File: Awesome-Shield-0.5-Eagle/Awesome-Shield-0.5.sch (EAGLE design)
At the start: 18 parts, among them J1 ARDUINO_R3_SHIELDUNO_R3_SHIEL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, P3 DNP, P4 DNP, SW1 SPST_TACT-EVQQ2

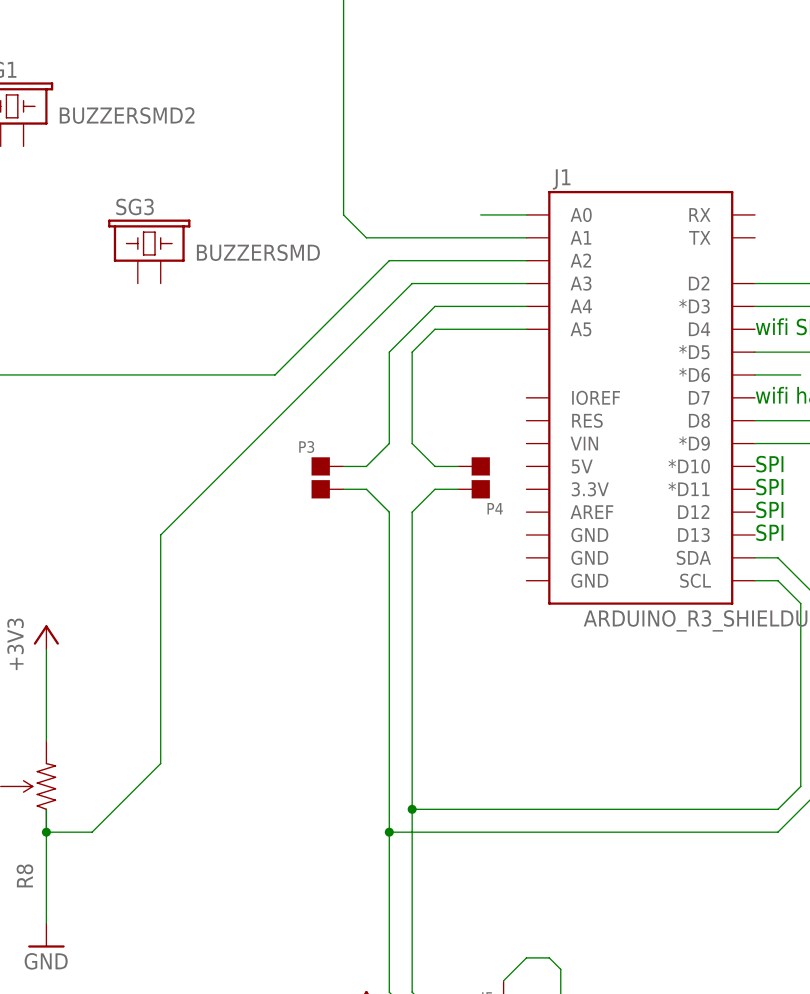
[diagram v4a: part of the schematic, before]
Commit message: switched jumpers to cutable traces
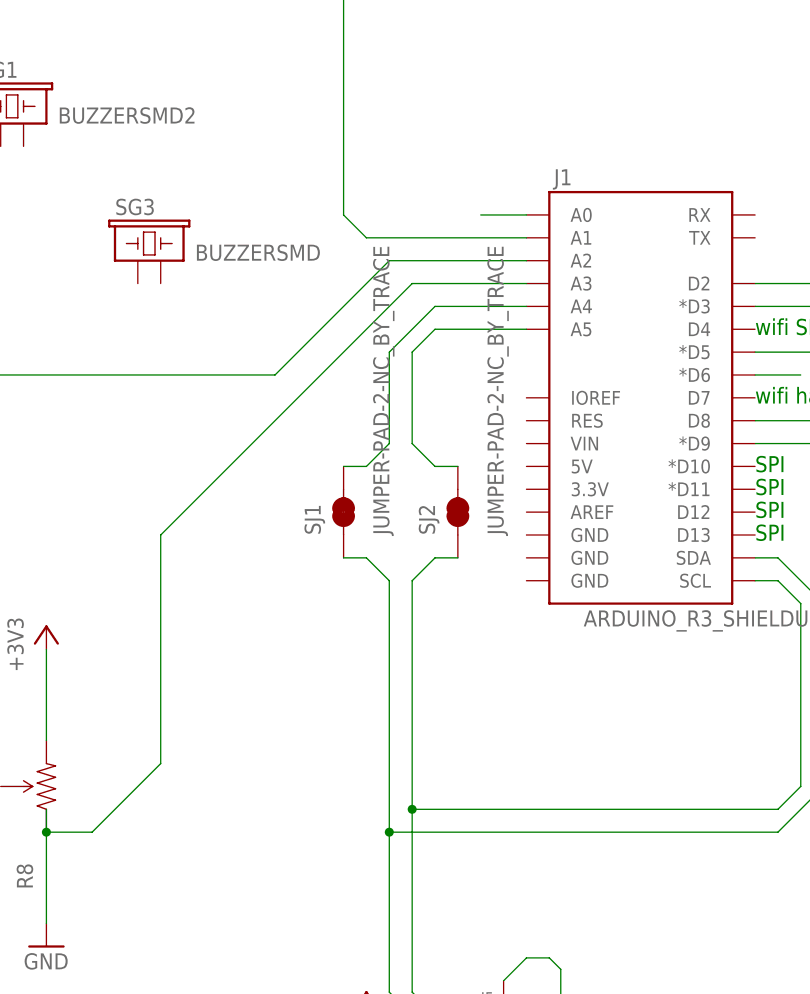
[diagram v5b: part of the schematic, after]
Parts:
- removed P3, P4: DNP, Discrete:PAD-JUMPER-2P
- added SJ1, SJ2: JUMPER-PAD-2-NC_BY_TRACE, SparkFun-Passives:JUMPER-PAD-2-NC_BY_TRACE
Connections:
- net A4: now also SJ1.2; no longer P3.2
- net A5: now also SJ2.2; no longer P4.1
- net SCL: now also SJ2.1; no longer P4.2
- net SDA: now also SJ1.1; no longer P3.1
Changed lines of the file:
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@@
 <part name="SG1" library="SparkFun-Electromechanical" deviceset="BUZZER" device="SMD2"/>
 <part name="SG3" library="SparkFun-Electromechanical" deviceset="BUZZER" device="SMD"/>
-<part name="P3" library="Discrete" deviceset="PAD-JUMPER-2P" device="" value="DNP"/>
-<part name="P4" library="Discrete" deviceset="PAD-JUMPER-2P" device="" value="DNP"/>
+<part name="SJ1" library="SparkFun-Passives" deviceset="JUMPER-PAD-2-NC_BY_TRACE" device=""/>
+<part name="SJ2" library="SparkFun-Passives" deviceset="JUMPER-PAD-2-NC_BY_TRACE" device=""/>
 </parts>
 <sheets>
@@
 <instance part="SG1" gate="G$1" x="124.46" y="160.02"/>
 <instance part="SG3" gate="G$1" x="139.7" y="144.78"/>
-<instance part="P3" gate="G$1" x="160.02" y="120.65"/>
-<instance part="P4" gate="G$1" x="177.8" y="120.65" rot="R180"/>
+<instance part="SJ1" gate="G$1" x="162.56" y="116.84" rot="R90"/>
+<instance part="SJ2" gate="G$1" x="175.26" y="116.84" rot="R90"/>
 </instances>
 <busses>
@@
 <segment>
 <wire x1="165.1" y1="121.92" x2="162.56" y2="121.92" width="0.1524" layer="91"/>
-<pinref part="P3" gate="G$1" pin="2"/>
 <wire x1="167.64" y1="124.46" x2="165.1" y2="121.92" width="0.1524" layer="91"/>
 <pinref part="J1" gate="G$1" pin="A4"/>
@@
 <wire x1="167.64" y1="134.62" x2="172.72" y2="139.7" width="0.1524" layer="91"/>
 <wire x1="167.64" y1="124.46" x2="167.64" y2="134.62" width="0.1524" layer="91"/>
+<pinref part="SJ1" gate="G$1" pin="2"/>
 </segment>
 </net>
@@
 <segment>
 <wire x1="170.18" y1="124.46" x2="172.72" y2="121.92" width="0.1524" layer="91"/>
-<pinref part="P4" gate="G$1" pin="1"/>
 <wire x1="172.72" y1="121.92" x2="175.26" y2="121.92" width="0.1524" layer="91"/>
 <pinref part="J1" gate="G$1" pin="A5"/>
@@
 <wire x1="172.72" y1="137.16" x2="170.18" y2="134.62" width="0.1524" layer="91"/>
 <wire x1="170.18" y1="134.62" x2="170.18" y2="124.46" width="0.1524" layer="91"/>
+<pinref part="SJ2" gate="G$1" pin="2"/>
 </segment>
 </net>
 <net name="SCL" class="0">
 <segment>
-<pinref part="P4" gate="G$1" pin="2"/>
-<wire x1="175.26" y1="119.38" x2="172.72" y2="119.38" width="0.1524" layer="91"/>
-<wire x1="172.72" y1="119.38" x2="170.18" y2="116.84" width="0.1524" layer="91"/>
-<wire x1="170.18" y1="116.84" x2="170.18" y2="83.82" width="0.1524" layer="91"/>
+<wire x1="175.26" y1="111.76" x2="172.72" y2="111.76" width="0.1524" layer="91"/>
+<wire x1="172.72" y1="111.76" x2="170.18" y2="109.22" width="0.1524" layer="91"/>
+<wire x1="170.18" y1="109.22" x2="170.18" y2="83.82" width="0.1524" layer="91"/>
 <pinref part="J5" gate="G$1" pin="1"/>
 <wire x1="170.18" y1="63.5" x2="172.72" y2="60.96" width="0.1524" layer="91"/>
@@
 <wire x1="213.36" y1="106.68" x2="213.36" y2="86.36" width="0.1524" layer="91"/>
 <wire x1="213.36" y1="86.36" x2="210.82" y2="83.82" width="0.1524" layer="91"/>
+<pinref part="SJ2" gate="G$1" pin="1"/>
 </segment>
 </net>
 <net name="SDA" class="0">
 <segment>
-<wire x1="162.56" y1="119.38" x2="165.1" y2="119.38" width="0.1524" layer="91"/>
-<wire x1="165.1" y1="119.38" x2="167.64" y2="116.84" width="0.1524" layer="91"/>
-<wire x1="167.64" y1="116.84" x2="167.64" y2="81.28" width="0.1524" layer="91"/>
-<pinref part="P3" gate="G$1" pin="1"/>
+<wire x1="162.56" y1="111.76" x2="165.1" y2="111.76" width="0.1524" layer="91"/>
+<wire x1="165.1" y1="111.76" x2="167.64" y2="109.22" width="0.1524" layer="91"/>
+<wire x1="167.64" y1="109.22" x2="167.64" y2="81.28" width="0.1524" layer="91"/>
 <pinref part="J5" gate="G$1" pin="2"/>
 <wire x1="172.72" y1="58.42" x2="167.64" y2="63.5" width="0.1524" layer="91"/>
@@
 <wire x1="215.9" y1="106.68" x2="215.9" y2="86.36" width="0.1524" layer="91"/>
 <wire x1="215.9" y1="86.36" x2="210.82" y2="81.28" width="0.1524" layer="91"/>
-</segment>
-</net>
+<pinref part="SJ1" gate="G$1" pin="1"/>
+</segment>
+</net>

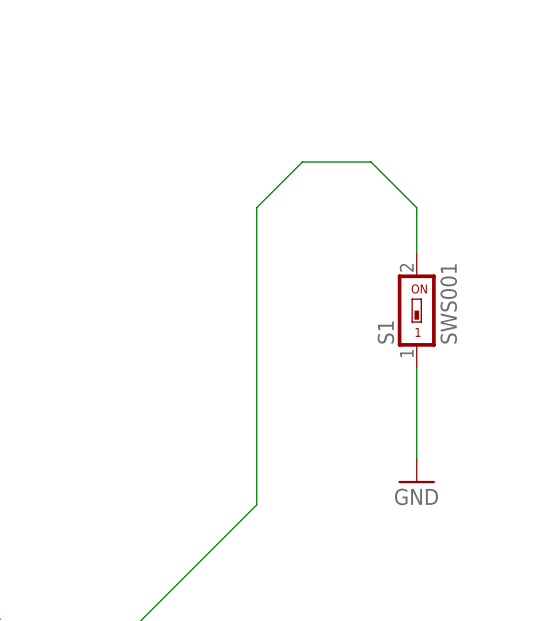
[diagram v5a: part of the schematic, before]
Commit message: redid toggle switch landing areas
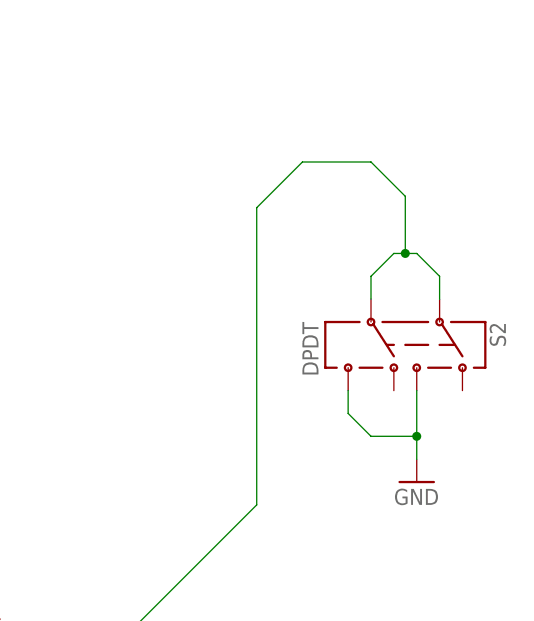
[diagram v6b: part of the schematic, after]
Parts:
- removed S1: SWS001, smd-special:SWS001
- added S2: DPDT, SparkFun-Electromechanical:SWITCH-DPDTAYZ0202
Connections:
- removed net N$1: J1.D8, S1.2
- new net N$6: J1.D8, S2.2, S2.5
- net GND: now also S2.3, S2.6; no longer S1.1
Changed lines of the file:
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@@
 <part name="J2" library="Connector " deviceset="TWIG-4P-2.0-SMD-FEMALE-REINFORCE" device="'DD'"/>
 <part name="GND10" library="supply1" deviceset="GND" device=""/>
-<part name="S1" library="smd-special" deviceset="SWS001" device=""/>
 <part name="GND12" library="supply1" deviceset="GND" device=""/>
 <part name="SG1" library="SparkFun-Electromechanical" deviceset="BUZZER" device="SMD2"/>
@@
 <part name="SJ1" library="SparkFun-Passives" deviceset="JUMPER-PAD-2-NC_BY_TRACE" device=""/>
 <part name="SJ2" library="SparkFun-Passives" deviceset="JUMPER-PAD-2-NC_BY_TRACE" device=""/>
+<part name="S2" library="SparkFun-Electromechanical" deviceset="SWITCH-DPDT" device="AYZ0202" value="DPDT"/>
 </parts>
 <sheets>
@@
 <instance part="J2" gate="G$1" x="287.02" y="85.09"/>
 <instance part="GND10" gate="1" x="287.02" y="71.12"/>
-<instance part="S1" gate="G$1" x="337.82" y="157.48"/>
 <instance part="GND12" gate="1" x="337.82" y="139.7"/>
 <instance part="SG1" gate="G$1" x="124.46" y="160.02"/>
@@
 <instance part="SJ1" gate="G$1" x="162.56" y="116.84" rot="R90"/>
 <instance part="SJ2" gate="G$1" x="175.26" y="116.84" rot="R90"/>
+<instance part="S2" gate="G$1" x="337.82" y="154.94" rot="R270"/>
 </instances>
 <busses>
@@
 </segment>
 <segment>
+<pinref part="S2" gate="G$1" pin="6"/>
+<wire x1="330.2" y1="149.86" x2="330.2" y2="147.32" width="0.1524" layer="91"/>
+<wire x1="330.2" y1="147.32" x2="332.74" y2="144.78" width="0.1524" layer="91"/>
+<wire x1="332.74" y1="144.78" x2="337.82" y2="144.78" width="0.1524" layer="91"/>
 <pinref part="GND12" gate="1" pin="GND"/>
-<wire x1="337.82" y1="142.24" x2="337.82" y2="152.4" width="0.1524" layer="91"/>
-<pinref part="S1" gate="G$1" pin="1"/>
+<wire x1="337.82" y1="144.78" x2="337.82" y2="142.24" width="0.1524" layer="91"/>
+<pinref part="S2" gate="G$1" pin="3"/>
+<wire x1="337.82" y1="144.78" x2="337.82" y2="149.86" width="0.1524" layer="91"/>
+<junction x="337.82" y="144.78"/>
 </segment>
 </net>
@@
 </segment>
 </net>
-<net name="N$1" class="0">
-<segment>
-<pinref part="J1" gate="G$1" pin="D8"/>
-<wire x1="208.28" y1="127" x2="254" y2="127" width="0.1524" layer="91"/>
-<wire x1="254" y1="127" x2="266.7" y2="114.3" width="0.1524" layer="91"/>
-<wire x1="266.7" y1="114.3" x2="297.18" y2="114.3" width="0.1524" layer="91"/>
-<wire x1="297.18" y1="114.3" x2="320.04" y2="137.16" width="0.1524" layer="91"/>
-<wire x1="320.04" y1="137.16" x2="320.04" y2="170.18" width="0.1524" layer="91"/>
-<pinref part="S1" gate="G$1" pin="2"/>
-<wire x1="337.82" y1="165.1" x2="337.82" y2="170.18" width="0.1524" layer="91"/>
-<wire x1="337.82" y1="170.18" x2="332.74" y2="175.26" width="0.1524" layer="91"/>
-<wire x1="332.74" y1="175.26" x2="325.12" y2="175.26" width="0.1524" layer="91"/>
-<wire x1="325.12" y1="175.26" x2="320.04" y2="170.18" width="0.1524" layer="91"/>
-</segment>
-</net>
 <net name="A0" class="0">
 <segment>
@@
 </segment>
 </net>
+<net name="N$6" class="0">
+<segment>
+<pinref part="S2" gate="G$1" pin="2"/>
+<wire x1="340.36" y1="162.56" x2="340.36" y2="160.02" width="0.1524" layer="91"/>
+<wire x1="337.82" y1="165.1" x2="340.36" y2="162.56" width="0.1524" layer="91"/>
+<wire x1="337.82" y1="165.1" x2="336.55" y2="165.1" width="0.1524" layer="91"/>
+<wire x1="336.55" y1="165.1" x2="335.28" y2="165.1" width="0.1524" layer="91"/>
+<wire x1="335.28" y1="165.1" x2="332.74" y2="162.56" width="0.1524" layer="91"/>
+<wire x1="332.74" y1="162.56" x2="332.74" y2="160.02" width="0.1524" layer="91"/>
+<pinref part="S2" gate="G$1" pin="5"/>
+<pinref part="J1" gate="G$1" pin="D8"/>
+<wire x1="208.28" y1="127" x2="254" y2="127" width="0.1524" layer="91"/>
+<wire x1="254" y1="127" x2="266.7" y2="114.3" width="0.1524" layer="91"/>
+<wire x1="266.7" y1="114.3" x2="297.18" y2="114.3" width="0.1524" layer="91"/>
+<wire x1="297.18" y1="114.3" x2="320.04" y2="137.16" width="0.1524" layer="91"/>
+<wire x1="320.04" y1="137.16" x2="320.04" y2="170.18" width="0.1524" layer="91"/>
+<wire x1="336.55" y1="171.45" x2="332.74" y2="175.26" width="0.1524" layer="91"/>
+<wire x1="332.74" y1="175.26" x2="325.12" y2="175.26" width="0.1524" layer="91"/>
+<wire x1="325.12" y1="175.26" x2="320.04" y2="170.18" width="0.1524" layer="91"/>
+<wire x1="336.55" y1="165.1" x2="336.55" y2="171.45" width="0.1524" layer="91"/>
+<junction x="336.55" y="165.1"/>
+</segment>
+</net>

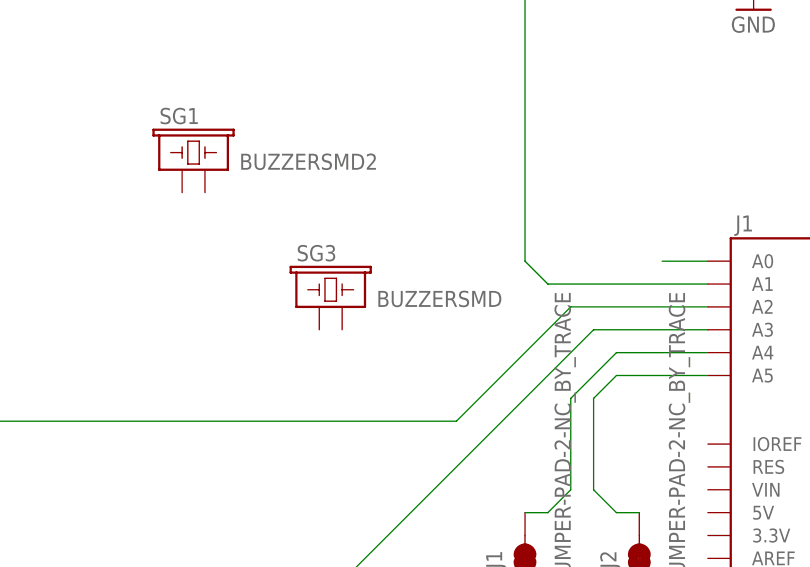
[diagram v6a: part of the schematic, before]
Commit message: removed extraneous buzzer
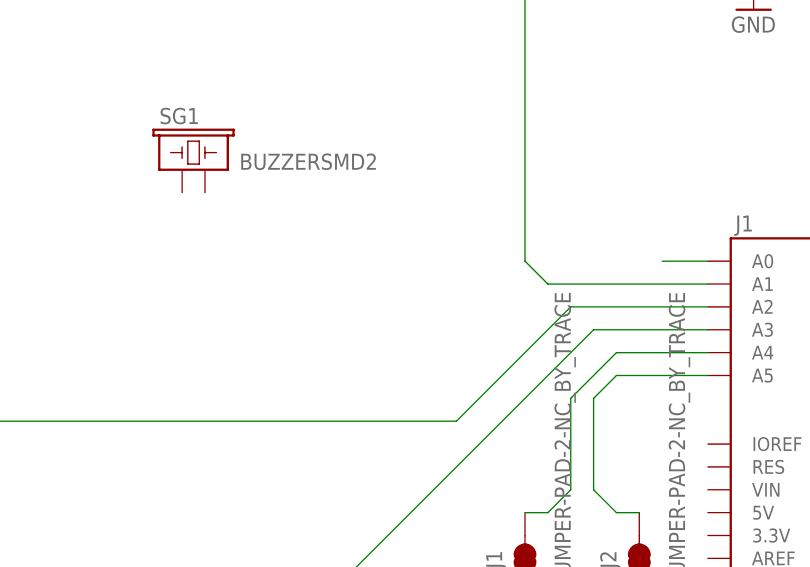
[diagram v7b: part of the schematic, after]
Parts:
- removed SG3: BUZZERSMD, SparkFun-Electromechanical:BUZZERSMD
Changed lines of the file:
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@@
 <part name="GND12" library="supply1" deviceset="GND" device=""/>
 <part name="SG1" library="SparkFun-Electromechanical" deviceset="BUZZER" device="SMD2"/>
-<part name="SG3" library="SparkFun-Electromechanical" deviceset="BUZZER" device="SMD"/>
 <part name="SJ1" library="SparkFun-Passives" deviceset="JUMPER-PAD-2-NC_BY_TRACE" device=""/>
 <part name="SJ2" library="SparkFun-Passives" deviceset="JUMPER-PAD-2-NC_BY_TRACE" device=""/>
@@
 <instance part="GND12" gate="1" x="337.82" y="139.7"/>
 <instance part="SG1" gate="G$1" x="124.46" y="160.02"/>
-<instance part="SG3" gate="G$1" x="139.7" y="144.78"/>
 <instance part="SJ1" gate="G$1" x="162.56" y="116.84" rot="R90"/>
 <instance part="SJ2" gate="G$1" x="175.26" y="116.84" rot="R90"/>
